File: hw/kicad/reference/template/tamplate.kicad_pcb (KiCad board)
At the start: 2 copper layers, 45 x 45 mm, 2 parts, among them J2 TOP, J4 BUTTOM

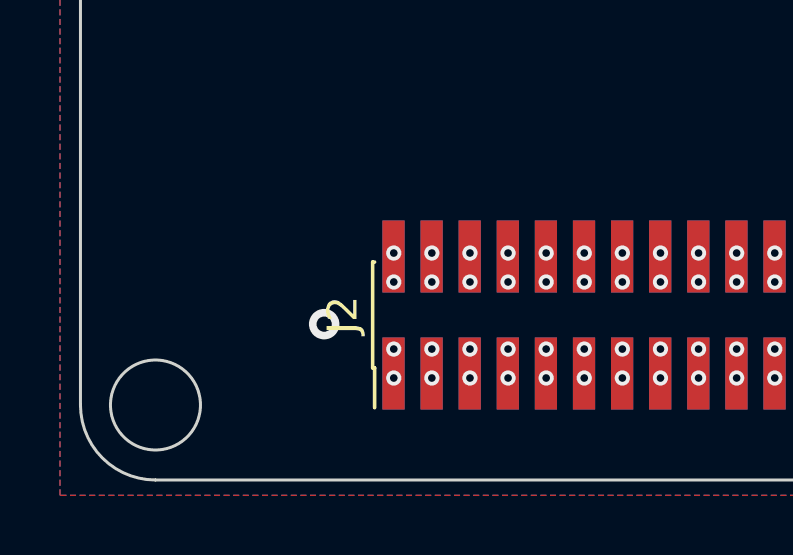
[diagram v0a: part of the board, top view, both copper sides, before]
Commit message: 更换接口线序
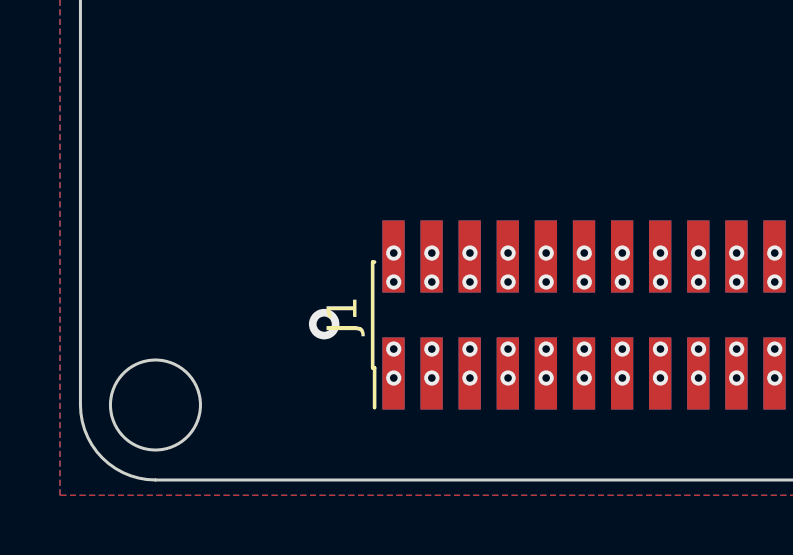
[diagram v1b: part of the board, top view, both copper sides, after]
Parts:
- removed J4: BUTTOM, Connector_PinHeader_1.27mm:PinHeader_2x20_P1.27mm_Vertical_SMD
- added J1: Conn_02x20_Odd_Even, Connector_PinHeader_1.27mm:PinHeader_2x20_P1.27mm_Vertical_SMD, F.Cu at (73.2, 72.2)
- J2: value TOP -> Conn_02x20_Odd_Even; moved to B.Cu
- turned J2 to -90 degrees
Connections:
- net /+BATT renamed /VBAT
- J2 pad 1: /ADC_1 -> /ADC_2
- J2 pad 10: /I2C_CLK -> /I2C_SDA
- J2 pad 11: /SPI_CS -> /SPI_CLK
- J2 pad 12: /SPI_CLK -> /SPI_CS
- J2 pad 13: /SPI_MOSI -> /SPI_MISO
- J2 pad 14: /SPI_MISO -> /SPI_MOSI
- J2 pad 15: /PWM_1 -> /CAN_L
- J2 pad 16: /PWM_2 -> /CAN_H
- J2 pad 17: /PWM_3 -> /USB-
- J2 pad 18: /PWM_4 -> /USB+
- J2 pad 19: /PWM_5 -> /GPIO_2
- J2 pad 2: /ADC_2 -> /ADC_1
- J2 pad 20: /PWM_6 -> /GPIO_1
- J2 pad 21: /PWM_7 -> /GPIO_4
- J2 pad 22: /PWM_8 -> /GPIO_3
- J2 pad 23: /CAN_H -> /GPIO_6
- J2 pad 24: /CAN_L -> /GPIO_5
- J2 pad 25: /USB+ -> /GPIO_8
- J2 pad 26: /USB- -> /GPIO_7
- J2 pad 3: /ADC_3 -> /ADC_4
- J2 pad 4: /ADC_4 -> /ADC_3
- J2 pad 5: /UART1_RX -> /UART1_TX
- J2 pad 6: /UART1_TX -> /UART1_RX
- J2 pad 7: /UART2_RX -> /UART2_TX
- J2 pad 8: /UART2_TX -> /UART2_RX
- J2 pad 9: /I2C_SDA -> /I2C_CLK
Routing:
- net /PWM_8: vias 2 -> 0
- net /PWM_7: vias 2 -> 0
- net /PWM_6: vias 2 -> 0
- net /PWM_5: vias 2 -> 0
- net /PWM_4: vias 2 -> 0
- net /PWM_3: vias 2 -> 0
- net /PWM_2: vias 2 -> 0
- net /PWM_1: vias 2 -> 0
- net /GPIO_8: vias 0 -> 2
- net /GPIO_7: vias 0 -> 2
- net /GPIO_6: vias 0 -> 2
- net /GPIO_5: vias 0 -> 2
- net /GPIO_4: vias 0 -> 2
- net /GPIO_3: vias 0 -> 2
- net /GPIO_2: vias 0 -> 2
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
